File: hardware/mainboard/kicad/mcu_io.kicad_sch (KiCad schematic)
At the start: 29 parts, among them J2 Hirose DM3AT-SF-PEJM5, SW2 BOOT / RECOVERY, SW3 BTN_L1, SW4 BTN_L2, SW5 BTN_R1, SW6 BTN_R2, U1 ESP32-S3-WROOM-1-N16R8, U5 BMI270, U6 DRV5032FBDBZR

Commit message: R28: separate Base and Pro hardware; remove Hall U6 and C20 and Qi markings from Base PCB
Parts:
- removed C20: 100nF, Capacitor_SMD:C_0603_1608Metric, symbol ENKU:C
- removed U6: DRV5032FBDBZR, Package_TO_SOT_SMD:SOT-23, symbol ENKU:DRV5032FB
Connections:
- net HALL_INT: no longer names the net of U1.10 (GPIO17)
- no-connect marks 19 -> 20
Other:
- note added: "BASE R28: Dedicated PCB - Hall sensor and cover circuitry removed (not DNP); no wireless charging, no frontlight. Separate Pro PCB."
- note removed: "Hall baseline frozen to DRV5032FBDBZR: 5Hz omnipolar push-pull SOT-23, chosen for cover-polarity tolerance and sub-uA class operation."
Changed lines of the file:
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@@
 	(global_label "CHG_STAT1" (shape input) (at 60.96 76.2 0) (effects (font (size 0.88 0.88)) (justify right bottom)))
 	(no_connect (at 60.96 78.74))
-	(global_label "HALL_INT" (shape input) (at 60.96 81.28 0) (effects (font (size 0.88 0.88)) (justify right bottom)))
+	(no_connect (at 60.96 81.28))
 	(global_label "IMU_INT1" (shape input) (at 60.96 83.82 0) (effects (font (size 0.88 0.88)) (justify right bottom)))
 	(global_label "I2C_SDA" (shape input) (at 60.96 86.36 0) (effects (font (size 0.88 0.88)) (justify right bottom)))
@@
 	(global_label "3V3_SYS" (shape input) (at 237.49 157.48 0) (effects (font (size 0.88 0.88)) (justify right bottom)))
 	(global_label "I2C_SCL" (shape output) (at 252.73 157.48 180) (effects (font (size 0.88 0.88)) (justify right bottom)))
-	(symbol (lib_id "ENKU:DRV5032FB") (at 249.555 62.23 0) (unit 1) (exclude_from_sim no) (in_bom yes) (on_board yes) (dnp no)
-		(property "Reference" "U6" (at 241.555 45.23 0) (effects (font (size 0.88 0.88))))
-		(property "Value" "DRV5032FBDBZR" (at 257.555 45.23 0) (effects (font (size 0.88 0.88))))
-		(property "Footprint" "Package_TO_SOT_SMD:SOT-23" (at 249.555 62.23 0) (effects (font (size 0.88 0.88)) (hide yes)))
-		(property "Datasheet" "~" (at 249.555 62.23 0) (effects (font (size 0.88 0.88)) (hide yes)))
-		(property "Description" "DRV5032FBDBZR" (at 249.555 62.23 0) (effects (font (size 0.88 0.88)) (hide yes)))
-		(pin "1")
-		(pin "2")
-		(pin "3")
-		(instances (project "enku-mainboard-r0.1" (path "/10000000-0000-4000-8000-000000000001/74000000-0000-4000-8000-000000000231" (reference "U6") (unit 1))))
-	)
-	(global_label "3V3_SYS" (shape input) (at 238.76 62.23 0) (effects (font (size 0.88 0.88)) (justify right bottom)))
-	(global_label "HALL_INT" (shape output) (at 260.35 60.96 180) (effects (font (size 0.88 0.88)) (justify right bottom)))
-	(global_label "GND" (shape output) (at 260.35 63.5 180) (effects (font (size 0.88 0.88)) (justify right bottom)))
-	(symbol (lib_id "ENKU:C") (at 250.19 87.63 0) (unit 1) (exclude_from_sim no) (in_bom yes) (on_board yes) (dnp no)
-		(property "Reference" "C20" (at 245.19 70.63 0) (effects (font (size 0.88 0.88))))
-		(property "Value" "100nF" (at 255.19 70.63 0) (effects (font (size 0.88 0.88))))
-		(property "Footprint" "Capacitor_SMD:C_0603_1608Metric" (at 250.19 87.63 0) (effects (font (size 0.88 0.88)) (hide yes)))
-		(property "Datasheet" "~" (at 250.19 87.63 0) (effects (font (size 0.88 0.88)) (hide yes)))
-		(property "Description" "100nF" (at 250.19 87.63 0) (effects (font (size 0.88 0.88)) (hide yes)))
-		(pin "1")
-		(pin "2")
-		(instances (project "enku-mainboard-r0.1" (path "/10000000-0000-4000-8000-000000000001/74000000-0000-4000-8000-000000000238" (reference "C20") (unit 1))))
-	)
-	(global_label "3V3_SYS" (shape input) (at 242.57 87.63 0) (effects (font (size 0.88 0.88)) (justify right bottom)))
-	(global_label "GND" (shape output) (at 257.81 87.63 180) (effects (font (size 0.88 0.88)) (justify right bottom)))
 	(symbol (lib_id "ENKU:R") (at 250.19 111.76 0) (unit 1) (exclude_from_sim no) (in_bom yes) (on_board yes) (dnp no)
 		(property "Reference" "R26" (at 245.19 94.76 0) (effects (font (size 0.88 0.88))))
@@
 	(global_label "GND" (shape input) (at 104.14 110.49 180) (effects (font (size 0.88 0.88)) (justify right bottom)))
 	(text "BMI270 is wired in I2C mode: SDO=GND (default address), CSB=3V3, VDD/VDDIO=3V3, INT1 only; unused secondary/OIS pins are NC." (exclude_from_sim no) (at 25 20 0) (effects (font (size 1.0 1.0)) (justify left bottom)))
-	(text "Hall baseline frozen to DRV5032FBDBZR: 5Hz omnipolar push-pull SOT-23, chosen for cover-polarity tolerance and sub-uA class operation." (exclude_from_sim no) (at 25 25 0) (effects (font (size 1.0 1.0)) (justify left bottom)))
+	(text "BASE R28: Dedicated PCB - Hall sensor and cover circuitry removed (not DNP); no wireless charging, no frontlight. Separate Pro PCB." (exclude_from_sim no) (at 25 25 0) (effects (font (size 1.0 1.0)) (justify left bottom)))
 	(text "microSD stays on shared SPI with independent CS and 0R/22R tuning links. DAT1/DAT2 unused in SPI mode." (exclude_from_sim no) (at 25 30 0) (effects (font (size 1.0 1.0)) (justify left bottom)))
 	(text "Battery ADC divider 2M/680k draws ~1.6uA at 4.2V; 100nF at ADC node provides acquisition charge reservoir. Validate ADC settling/calibration in firmware." (exclude_from_sim no) (at 25 35 0) (effects (font (size 1.0 1.0)) (justify left bottom)))

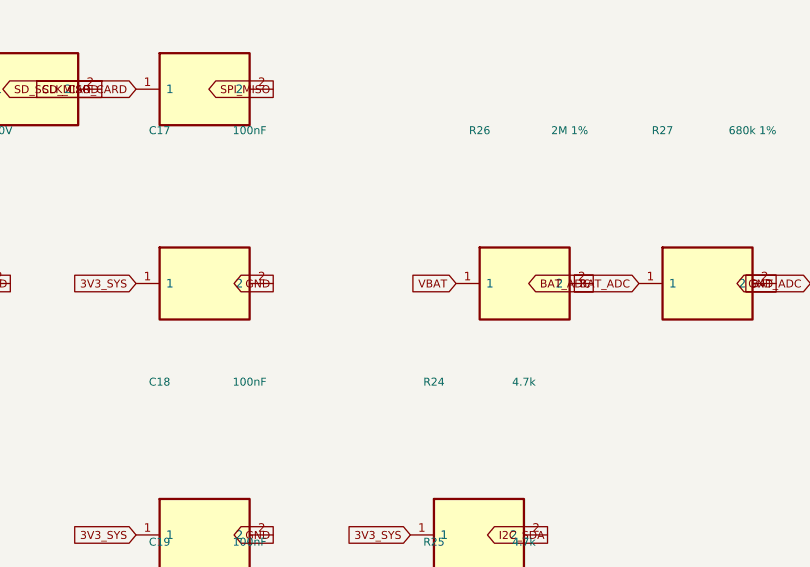
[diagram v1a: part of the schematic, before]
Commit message: R34: link TMUX1101 schematic symbol and isolate R26 battery-side divider net
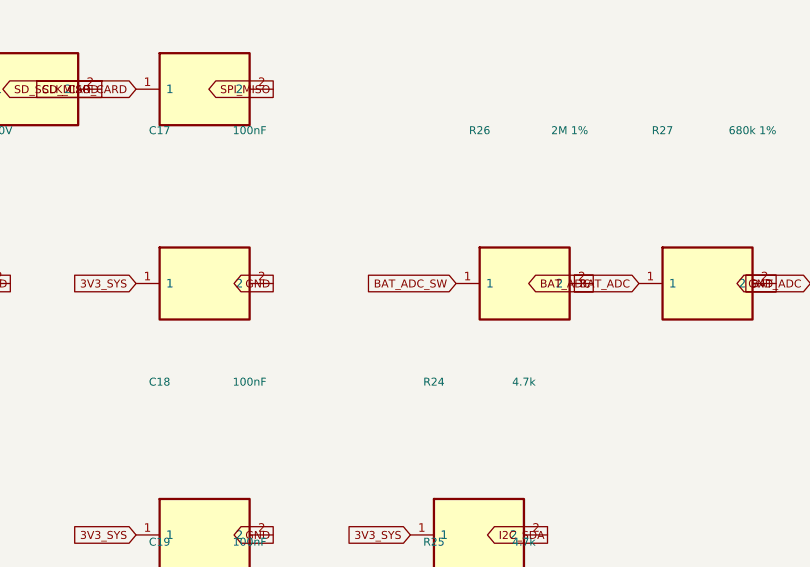
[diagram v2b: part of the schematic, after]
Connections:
- net VBAT renamed BAT_ADC_SW
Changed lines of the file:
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@@
 		(instances (project "enku-mainboard-r0.1" (path "/10000000-0000-4000-8000-000000000001/74000000-0000-4000-8000-000000000243" (reference "R26") (unit 1))))
 	)
-	(global_label "VBAT" (shape input) (at 242.57 111.76 0) (effects (font (size 0.88 0.88)) (justify right bottom)))
+	(global_label "BAT_ADC_SW" (shape input) (at 242.57 111.76 0) (effects (font (size 0.88 0.88)) (justify right bottom)))
 	(global_label "BAT_ADC" (shape output) (at 257.81 111.76 180) (effects (font (size 0.88 0.88)) (justify right bottom)))
 	(symbol (lib_id "ENKU:R") (at 270.51 111.76 0) (unit 1) (exclude_from_sim no) (in_bom yes) (on_board yes) (dnp no)

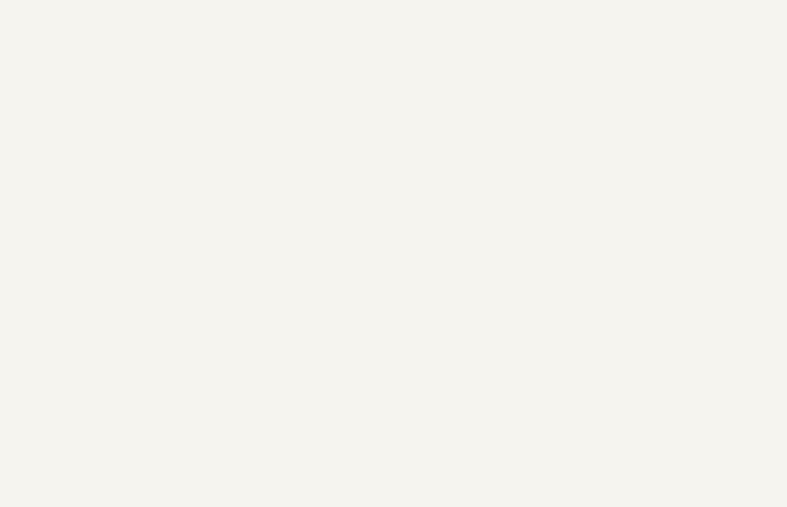
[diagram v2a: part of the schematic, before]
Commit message: R34: place U9 TMUX1101, C37 decoupler and R39 SEL pulldown with schematic nets
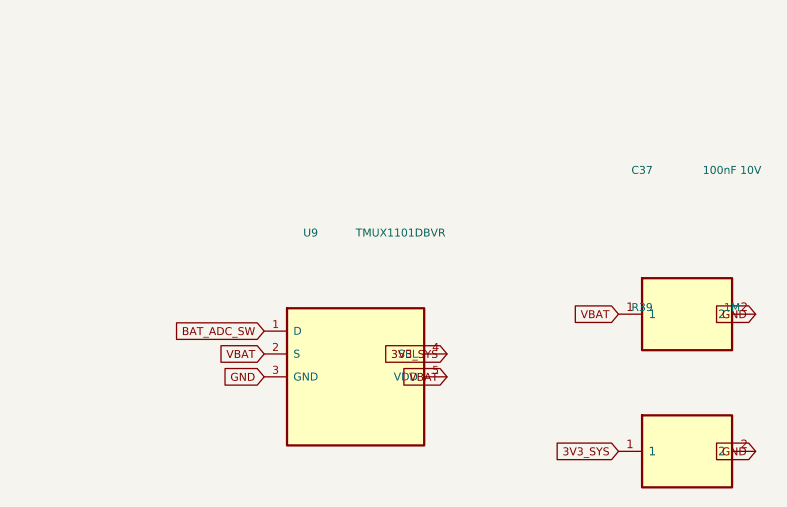
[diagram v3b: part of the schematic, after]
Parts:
- added C37: 100nF 10V, Capacitor_SMD:C_0603_1608Metric, symbol ENKU:C
- added R39: 1M, Resistor_SMD:R_0603_1608Metric, symbol ENKU:R
- added U9: TMUX1101DBVR, Package_TO_SOT_SMD:SOT-23-5, symbol ENKU:TMUX1101
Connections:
- net 3V3_SYS: now also R39.1, U9.4 (SEL)
- net BAT_ADC_SW: now also U9.1 (D)
- net GND: now also C37.2, R39.2, U9.3 (GND)
- new net VBAT: C37.1, U9.2 (S), U9.5 (VDD)
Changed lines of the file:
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@@
 	(text "Battery ADC divider 2M/680k draws ~1.6uA at 4.2V; 100nF at ADC node provides acquisition charge reservoir. Validate ADC settling/calibration in firmware." (exclude_from_sim no) (at 25 35 0) (effects (font (size 1.0 1.0)) (justify left bottom)))
 	(sheet_instances (path "/" (page "3")))
+	(symbol (lib_id "ENKU:TMUX1101") (at 330.2 174.6 0) (unit 1) (exclude_from_sim no) (in_bom yes) (on_board yes) (dnp no)
+(property "Reference" "U9" (at 325.2 158.6 0) (effects (font (size 0.88 0.88))))
+(property "Value" "TMUX1101DBVR" (at 335.2 158.6 0) (effects (font (size 0.88 0.88))))
+(property "Footprint" "Package_TO_SOT_SMD:SOT-23-5" (at 330.2 174.6 0) (effects (font (size 0.88 0.88)) (hide yes)))
+(property "Datasheet" "https://www.ti.com/lit/ds/symlink/tmux1101.pdf" (at 330.2 174.6 0) (effects (font (size 0.88 0.88)) (hide yes)))
+(property "Description" "TMUX1101DBVR" (at 330.2 174.6 0) (effects (font (size 0.88 0.88)) (hide yes)))
+(pin "1")
+(pin "2")
+(pin "3")
+(pin "4")
+(pin "5")
+(instances (project "enku-mainboard-r0.1" (path "/10000000-0000-4000-8000-000000000001/e4100000-0000-4000-8000-000000000001" (reference "U9") (unit 1))))
 )
+	(symbol (lib_id "ENKU:C") (at 367.03 167.64 0) (unit 1) (exclude_from_sim no) (in_bom yes) (on_board yes) (dnp no)
+(property "Reference" "C37" (at 362.03 151.64 0) (effects (font (size 0.88 0.88))))
+(property "Value" "100nF 10V" (at 372.03 151.64 0) (effects (font (size 0.88 0.88))))
+(property "Footprint" "Capacitor_SMD:C_0603_1608Metric" (at 367.03 167.64 0) (effects (font (size 0.88 0.88)) (hide yes)))
+(property "Datasheet" "~" (at 367.03 167.64 0) (effects (font (size 0.88 0.88)) (hide yes)))
+(property "Description" "100nF 10V" (at 367.03 167.64 0) (effects (font (size 0.88 0.88)) (hide yes)))
+(pin "1")
+(pin "2")
+(instances (project "enku-mainboard-r0.1" (path "/10000000-0000-4000-8000-000000000001/e4100000-0000-4000-8000-000000000020" (reference "C37") (unit 1))))
+)
+	(symbol (lib_id "ENKU:R") (at 367.03 182.88 0) (unit 1) (exclude_from_sim no) (in_bom yes) (on_board yes) (dnp no)
+(property "Reference" "R39" (at 362.03 166.88 0) (effects (font (size 0.88 0.88))))
+(property "Value" "1M" (at 372.03 166.88 0) (effects (font (size 0.88 0.88))))
+(property "Footprint" "Resistor_SMD:R_0603_1608Metric" (at 367.03 182.88 0) (effects (font (size 0.88 0.88)) (hide yes)))
+(property "Datasheet" "~" (at 367.03 182.88 0) (effects (font (size 0.88 0.88)) (hide yes)))
+(property "Description" "1M" (at 367.03 182.88 0) (effects (font (size 0.88 0.88)) (hide yes)))
+(pin "1")
+(pin "2")
+(instances (project "enku-mainboard-r0.1" (path "/10000000-0000-4000-8000-000000000001/e4100000-0000-4000-8000-000000000030" (reference "R39") (unit 1))))
+)
+	(global_label "BAT_ADC_SW" (shape input) (at 320.04 169.52 0) (effects (font (size 0.88 0.88)) (justify right bottom)))
+	(global_label "VBAT" (shape input) (at 320.04 172.06 0) (effects (font (size 0.88 0.88)) (justify right bottom)))
+	(global_label "GND" (shape input) (at 320.04 174.6 0) (effects (font (size 0.88 0.88)) (justify right bottom)))
+	(global_label "3V3_SYS" (shape input) (at 340.36 172.06 180) (effects (font (size 0.88 0.88)) (justify right bottom)))
+	(global_label "VBAT" (shape input) (at 340.36 174.6 180) (effects (font (size 0.88 0.88)) (justify right bottom)))
+	(global_label "VBAT" (shape input) (at 359.41 167.64 0) (effects (font (size 0.88 0.88)) (justify right bottom)))
+	(global_label "GND" (shape input) (at 374.65 167.64 180) (effects (font (size 0.88 0.88)) (justify right bottom)))
+	(global_label "3V3_SYS" (shape input) (at 359.41 182.88 0) (effects (font (size 0.88 0.88)) (justify right bottom)))
+	(global_label "GND" (shape input) (at 374.65 182.88 180) (effects (font (size 0.88 0.88)) (justify right bottom)))
+)
